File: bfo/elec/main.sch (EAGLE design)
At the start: 10 parts, among them Q1 BC108B

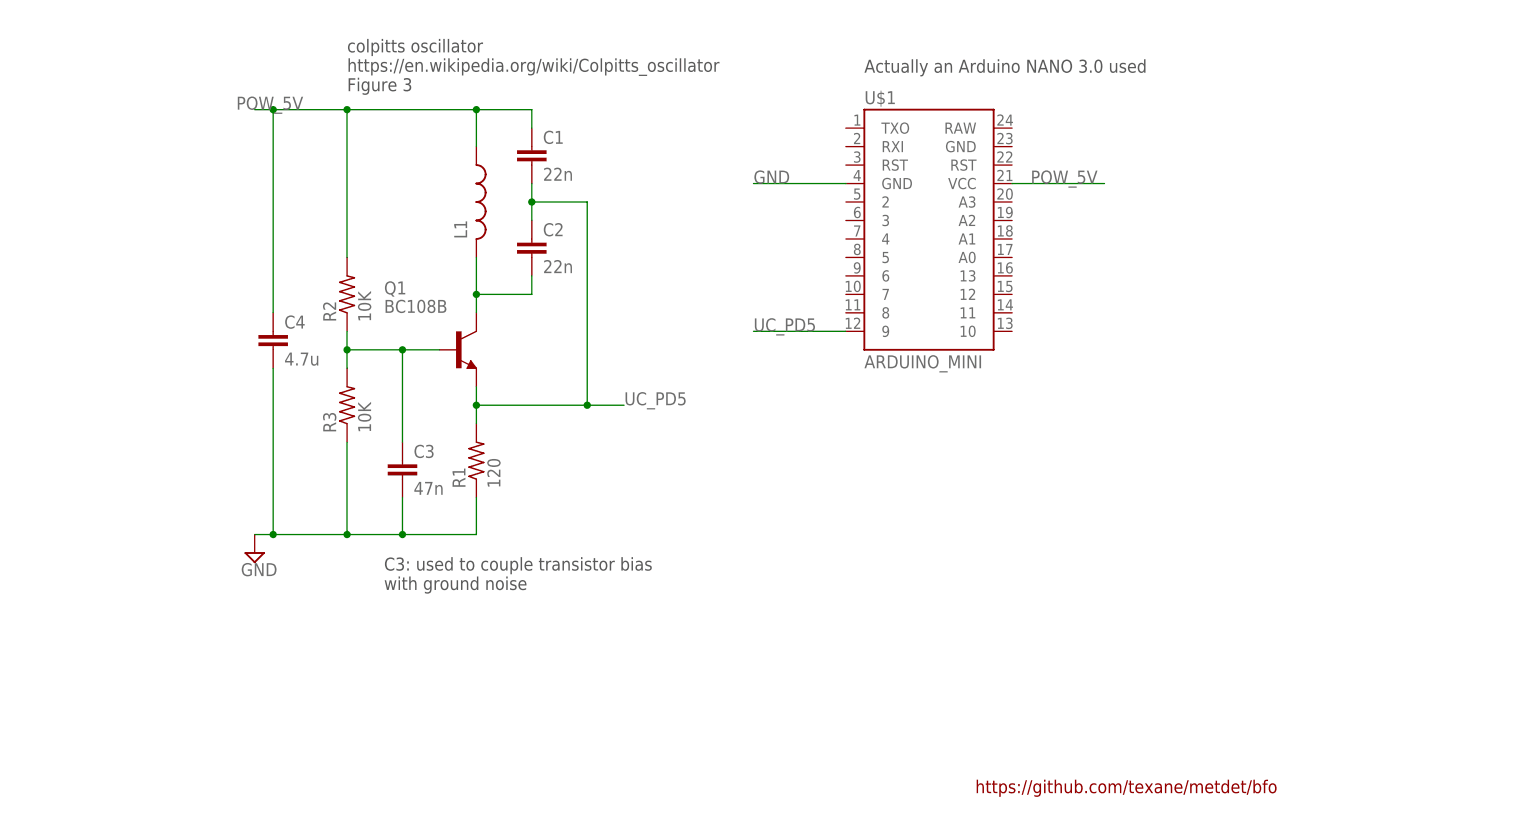
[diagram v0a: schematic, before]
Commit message: bfo/elec: add inverter stage
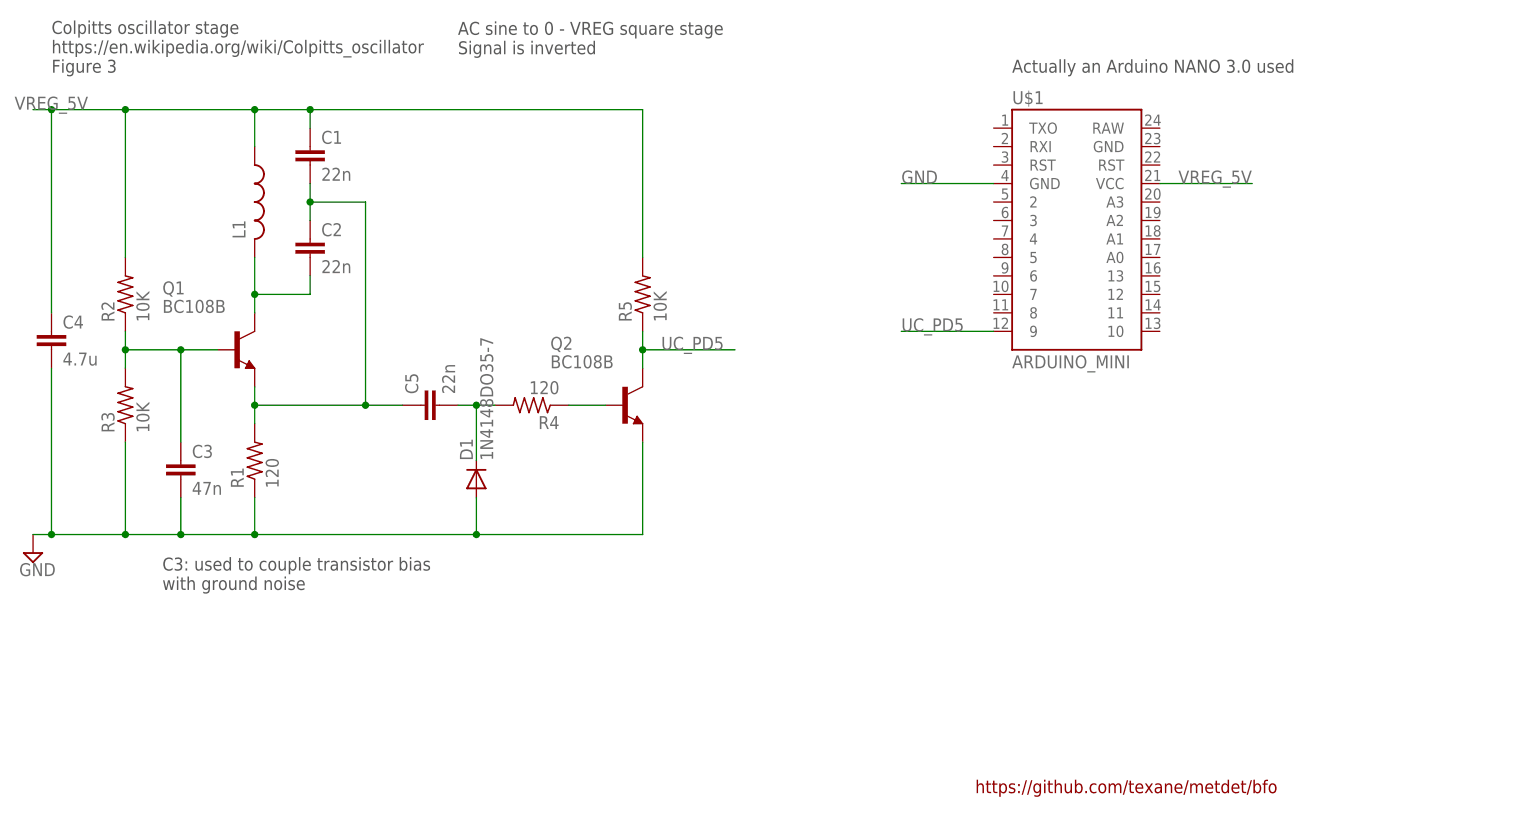
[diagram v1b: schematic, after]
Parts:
- added C5: 22n, rcl:C-EU025-024X044
- added D1: 1N4148DO35-7, diode:1N4148DO35-7
- added Q2: BC108B, transistor-npn:BC108B
- added R4: 120, rcl:R-US_0204/2V
- added R5: 10K, rcl:R-US_0204/2V
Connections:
- removed net POW_5V: C1.1, C4.1, L1.1, R2.2, U$1.VCC
- new net N$10: C1.2, C2.1, C5.1, Q1.E, R1.2
- new net N$5: Q2.B, R4.1
- new net N$6: C5.2, D1.C, R4.2
- new net VREG_5V: C1.1, C4.1, L1.1, R2.2, R5.2, U$1.VCC
- net GND: now also D1.A, Q2.E
- net UC_PD5: now also Q2.C, R5.1; no longer C1.2, C2.1, Q1.E, R1.2
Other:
- note added: "AC sine to 0 - VREG square stage Signal is inverted"
- note added: "Colpitts oscillator stage https://en.wikipedia.org/wiki/Colpitts_oscillator Figure 3"
- note removed: "colpitts oscillator https://en.wikipedia.org/wiki/Colpitts_oscillator Figure 3"
- moved on the sheet: C1, C2, C3, C4, L1, Q1, R1, R2, R3, U$1

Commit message: bfo/elec: comments
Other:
- note added: "AC sine to logic (0 - VREG, inverted)"
- note removed: "AC sine to 0 - VREG square stage Signal is inverted"
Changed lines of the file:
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@@
 <text x="114.3" y="58.42" size="1.778" layer="97">Actually an Arduino NANO 3.0 used</text>
 <text x="109.22" y="-40.64" size="1.778" layer="94">https://github.com/texane/metdet/bfo</text>
-<text x="38.1" y="60.96" size="1.778" layer="97">AC sine to 0 - VREG square stage
-Signal is inverted</text>
+<text x="38.1" y="58.42" size="1.778" layer="97">AC sine to logic (0 - VREG, inverted)</text>
 </plain>
 <instances>

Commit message: bfo/elec: add piezo buzzer
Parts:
- added SG1: EFBAA40D101, buzzer:EFBAA40D101
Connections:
- new net N$2: SG1.1, U$1.10
- net GND: now also SG1.2
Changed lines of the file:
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@@
 <part name="Q2" library="transistor-npn" deviceset="BC108B" device=""/>
 <part name="D1" library="diode" deviceset="1N4148" device="DO35-7"/>
+<part name="SG1" library="buzzer" deviceset="EFB?" device="AA40D101"/>
+<part name="SUPPLY2" library="supply2" deviceset="GND" device=""/>
 </parts>
 <sheets>
@@
 <instance part="Q2" gate="G$1" x="60.96" y="12.7"/>
 <instance part="D1" gate="G$1" x="40.64" y="2.54" rot="R90"/>
+<instance part="SG1" gate="G$1" x="144.78" y="25.4"/>
+<instance part="SUPPLY2" gate="GND" x="160.02" y="20.32"/>
 </instances>
 <busses>
@@
 <label x="99.06" y="43.18" size="1.778" layer="95"/>
 </segment>
+<segment>
+<pinref part="SG1" gate="G$1" pin="2"/>
+<wire x1="149.86" y1="22.86" x2="160.02" y2="22.86" width="0.1524" layer="91"/>
+<pinref part="SUPPLY2" gate="GND" pin="GND"/>
+</segment>
 </net>
 <net name="VREG_5V" class="0">
@@
 </segment>
 </net>
+<net name="N$2" class="0">
+<segment>
+<pinref part="U$1" gate="G$1" pin="10"/>
+<pinref part="SG1" gate="G$1" pin="1"/>
+<wire x1="134.62" y1="22.86" x2="142.24" y2="22.86" width="0.1524" layer="91"/>
+</segment>
+</net>

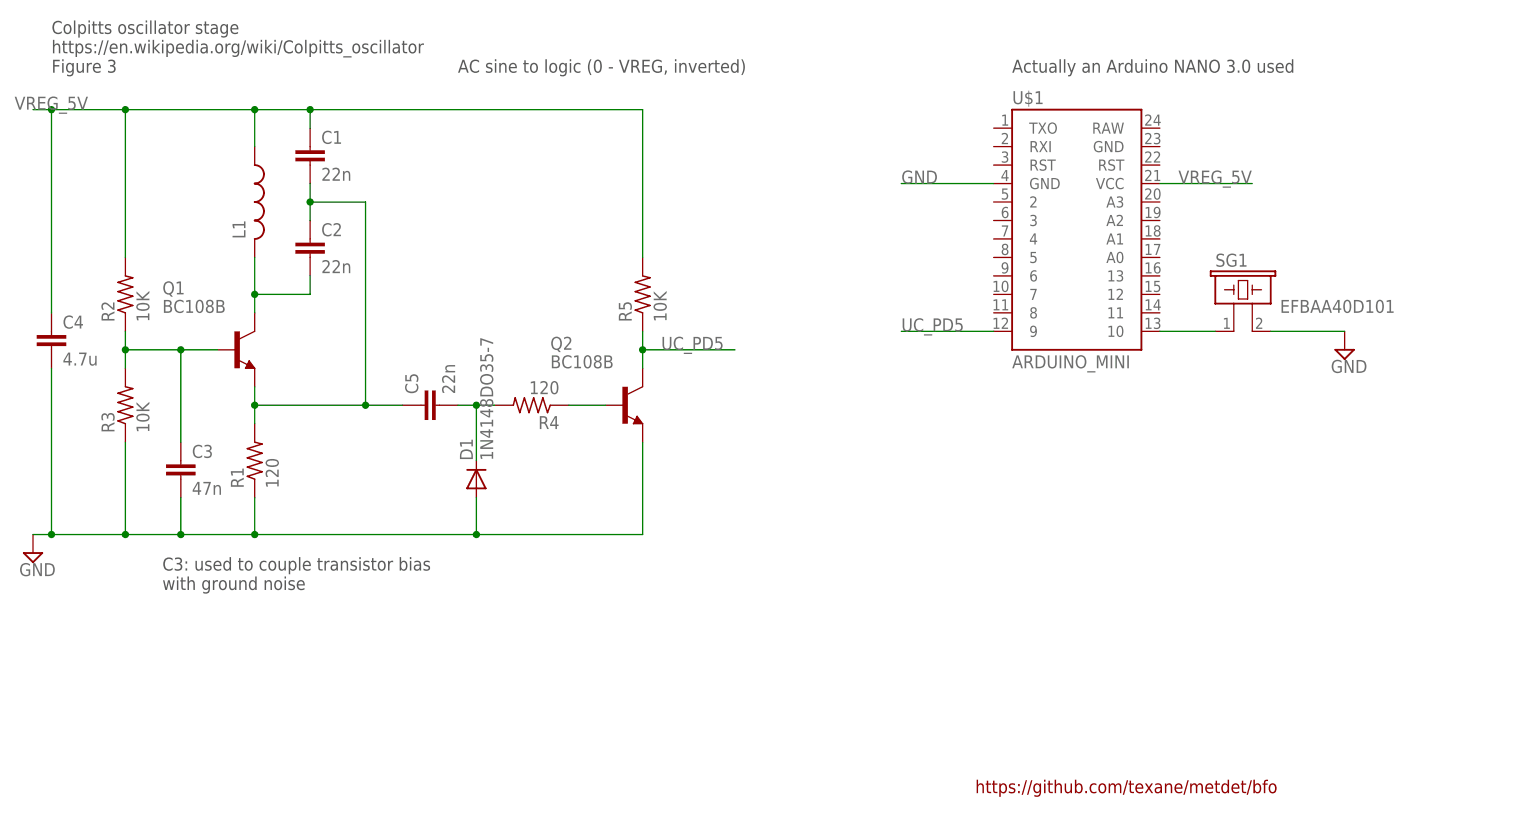
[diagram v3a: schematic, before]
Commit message: bfo/elec: add box connector
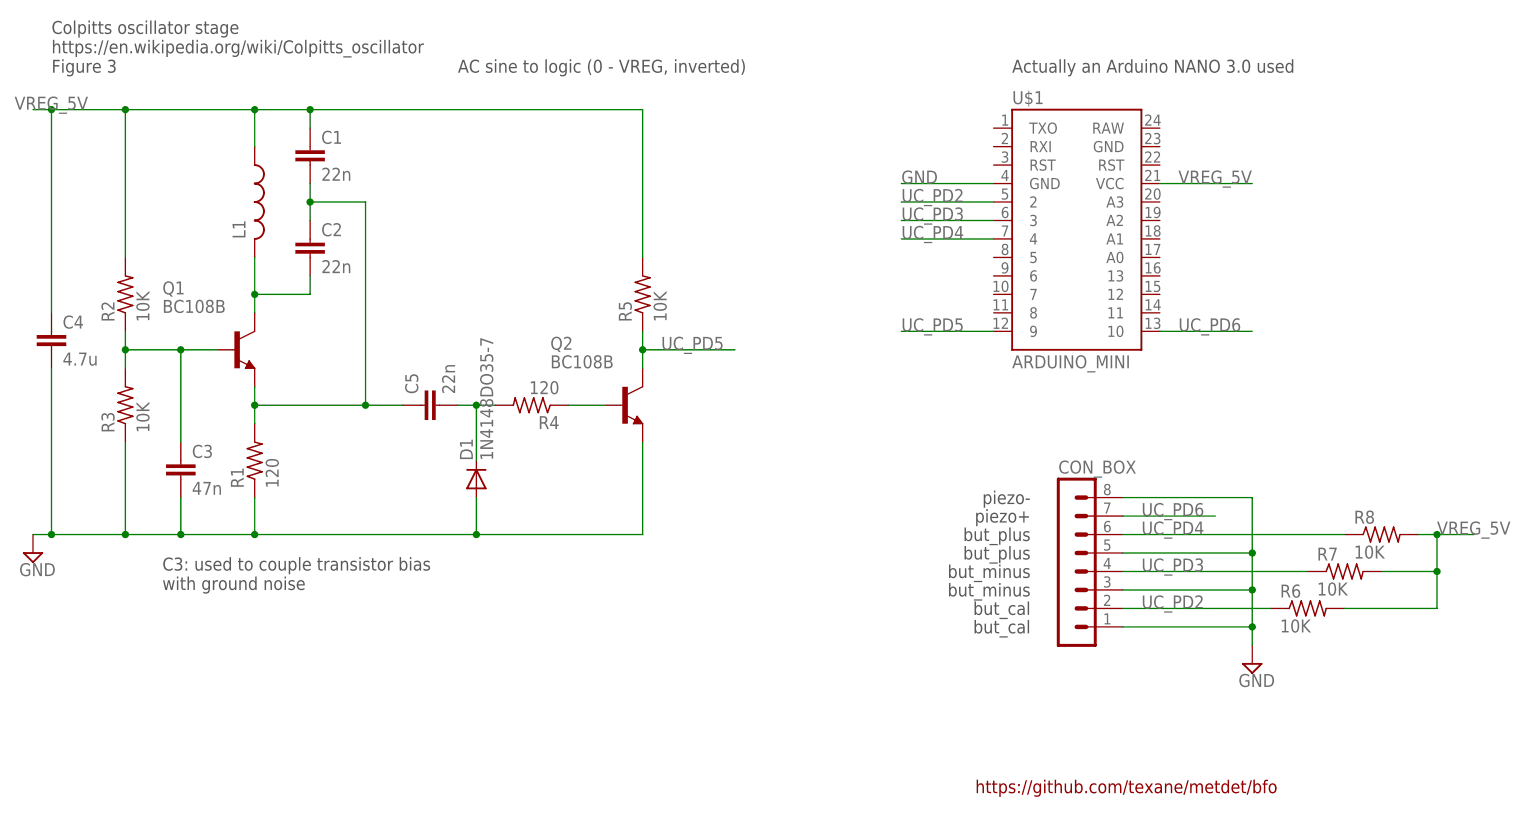
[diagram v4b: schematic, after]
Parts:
- removed SG1: EFBAA40D101, buzzer:EFBAA40D101
- added CON_BOX: (no value), con-lstb:MA08-1
- added R6, R7, R8: 10K, rcl:R-US_0204/2V
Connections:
- removed net N$2: SG1.1, U$1.10
- new net UC_PD2: CON_BOX.2, R6.1, U$1.2
- new net UC_PD3: CON_BOX.4, R7.1, U$1.3
- new net UC_PD4: CON_BOX.6, R8.1, U$1.4
- new net UC_PD6: CON_BOX.7, U$1.10
- net GND: now also CON_BOX.1, CON_BOX.3, CON_BOX.5, CON_BOX.8; no longer SG1.2
- net VREG_5V: now also R6.2, R7.2, R8.2
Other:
- note added: "but_cal"
- note added: "but_minus"
- note added: "but_plus"
- note added: "piezo+"
- note added: "piezo-"
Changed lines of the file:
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@@
 <part name="Q2" library="transistor-npn" deviceset="BC108B" device=""/>
 <part name="D1" library="diode" deviceset="1N4148" device="DO35-7"/>
-<part name="SG1" library="buzzer" deviceset="EFB?" device="AA40D101"/>
-<part name="SUPPLY2" library="supply2" deviceset="GND" device=""/>
+<part name="CON_BOX" library="con-lstb" deviceset="MA08-1" device=""/>
+<part name="R6" library="rcl" deviceset="R-US_" device="0204/2V" value="10K"/>
+<part name="R7" library="rcl" deviceset="R-US_" device="0204/2V" value="10K"/>
+<part name="R8" library="rcl" deviceset="R-US_" device="0204/2V" value="10K"/>
+<part name="SUPPLY4" library="supply2" deviceset="GND" device=""/>
 </parts>
 <sheets>
@@
 <text x="109.22" y="-40.64" size="1.778" layer="94">https://github.com/texane/metdet/bfo</text>
 <text x="38.1" y="58.42" size="1.778" layer="97">AC sine to logic (0 - VREG, inverted)</text>
+<text x="116.84" y="0" size="1.778" layer="97" align="center-right">piezo-</text>
+<text x="116.84" y="-2.54" size="1.778" layer="97" align="center-right">piezo+</text>
+<text x="116.84" y="-5.08" size="1.778" layer="97" align="center-right">but_plus</text>
+<text x="116.84" y="-7.62" size="1.778" layer="97" align="center-right">but_plus</text>
+<text x="116.84" y="-10.16" size="1.778" layer="97" align="center-right">but_minus</text>
+<text x="116.84" y="-12.7" size="1.778" layer="97" align="center-right">but_minus</text>
+<text x="116.84" y="-15.24" size="1.778" layer="97" align="center-right">but_cal</text>
+<text x="116.84" y="-17.78" size="1.778" layer="97" align="center-right">but_cal</text>
 </plain>
 <instances>
@@
 <instance part="Q2" gate="G$1" x="60.96" y="12.7"/>
 <instance part="D1" gate="G$1" x="40.64" y="2.54" rot="R90"/>
-<instance part="SG1" gate="G$1" x="144.78" y="25.4"/>
-<instance part="SUPPLY2" gate="GND" x="160.02" y="20.32"/>
+<instance part="CON_BOX" gate="1" x="121.92" y="-10.16"/>
+<instance part="R6" gate="G$1" x="154.94" y="-15.24"/>
+<instance part="R7" gate="G$1" x="160.02" y="-10.16"/>
+<instance part="R8" gate="G$1" x="165.1" y="-5.08"/>
+<instance part="SUPPLY4" gate="GND" x="147.32" y="-22.86"/>
 </instances>
 <busses>
@@
 </segment>
 <segment>
-<pinref part="SG1" gate="G$1" pin="2"/>
-<wire x1="149.86" y1="22.86" x2="160.02" y2="22.86" width="0.1524" layer="91"/>
-<pinref part="SUPPLY2" gate="GND" pin="GND"/>
+<pinref part="CON_BOX" gate="1" pin="5"/>
+<wire x1="129.54" y1="-7.62" x2="147.32" y2="-7.62" width="0.1524" layer="91"/>
+<pinref part="SUPPLY4" gate="GND" pin="GND"/>
+<wire x1="147.32" y1="-7.62" x2="147.32" y2="-12.7" width="0.1524" layer="91"/>
+<pinref part="CON_BOX" gate="1" pin="3"/>
+<wire x1="147.32" y1="-12.7" x2="147.32" y2="-17.78" width="0.1524" layer="91"/>
+<wire x1="147.32" y1="-17.78" x2="147.32" y2="-20.32" width="0.1524" layer="91"/>
+<wire x1="129.54" y1="-12.7" x2="147.32" y2="-12.7" width="0.1524" layer="91"/>
+<junction x="147.32" y="-12.7"/>
+<pinref part="CON_BOX" gate="1" pin="1"/>
+<wire x1="129.54" y1="-17.78" x2="147.32" y2="-17.78" width="0.1524" layer="91"/>
+<junction x="147.32" y="-17.78"/>
+<pinref part="CON_BOX" gate="1" pin="8"/>
+<wire x1="129.54" y1="0" x2="147.32" y2="0" width="0.1524" layer="91"/>
+<wire x1="147.32" y1="0" x2="147.32" y2="-7.62" width="0.1524" layer="91"/>
+<junction x="147.32" y="-7.62"/>
 </segment>
 </net>
@@
 <label x="137.16" y="43.18" size="1.778" layer="95"/>
 </segment>
+<segment>
+<pinref part="R8" gate="G$1" pin="2"/>
+<wire x1="170.18" y1="-5.08" x2="172.72" y2="-5.08" width="0.1524" layer="91"/>
+<wire x1="172.72" y1="-5.08" x2="172.72" y2="-10.16" width="0.1524" layer="91"/>
+<pinref part="R6" gate="G$1" pin="2"/>
+<wire x1="172.72" y1="-10.16" x2="172.72" y2="-15.24" width="0.1524" layer="91"/>
+<wire x1="172.72" y1="-15.24" x2="160.02" y2="-15.24" width="0.1524" layer="91"/>
+<pinref part="R7" gate="G$1" pin="2"/>
+<wire x1="165.1" y1="-10.16" x2="172.72" y2="-10.16" width="0.1524" layer="91"/>
+<junction x="172.72" y="-10.16"/>
+<wire x1="172.72" y1="-5.08" x2="177.8" y2="-5.08" width="0.1524" layer="91"/>
+<junction x="172.72" y="-5.08"/>
+<label x="172.72" y="-5.08" size="1.778" layer="95"/>
+</segment>
 </net>
 <net name="N$10" class="0">
@@
 </segment>
 </net>
-<net name="N$2" class="0">
+<net name="UC_PD6" class="0">
+<segment>
+<pinref part="CON_BOX" gate="1" pin="7"/>
+<wire x1="129.54" y1="-2.54" x2="142.24" y2="-2.54" width="0.1524" layer="91"/>
+<label x="132.08" y="-2.54" size="1.778" layer="95"/>
+</segment>
 <segment>
 <pinref part="U$1" gate="G$1" pin="10"/>
-<pinref part="SG1" gate="G$1" pin="1"/>
-<wire x1="134.62" y1="22.86" x2="142.24" y2="22.86" width="0.1524" layer="91"/>
-</segment>
-</net>
+<wire x1="134.62" y1="22.86" x2="147.32" y2="22.86" width="0.1524" layer="91"/>
+<label x="137.16" y="22.86" size="1.778" layer="95"/>
+</segment>
+</net>
+<net name="UC_PD2" class="0">
+<segment>
+<pinref part="U$1" gate="G$1" pin="2"/>
+<wire x1="111.76" y1="40.64" x2="99.06" y2="40.64" width="0.1524" layer="91"/>
+<label x="99.06" y="40.64" size="1.778" layer="95"/>
+</segment>
+<segment>
+<pinref part="R6" gate="G$1" pin="1"/>
+<pinref part="CON_BOX" gate="1" pin="2"/>
+<wire x1="149.86" y1="-15.24" x2="129.54" y2="-15.24" width="0.1524" layer="91"/>
+<label x="132.08" y="-15.24" size="1.778" layer="95"/>
+</segment>
+</net>
+<net name="UC_PD3" class="0">
+<segment>
+<pinref part="U$1" gate="G$1" pin="3"/>
+<wire x1="111.76" y1="38.1" x2="99.06" y2="38.1" width="0.1524" layer="91"/>
+<label x="99.06" y="38.1" size="1.778" layer="95"/>
+</segment>
+<segment>
+<pinref part="R7" gate="G$1" pin="1"/>
+<pinref part="CON_BOX" gate="1" pin="4"/>
+<wire x1="154.94" y1="-10.16" x2="129.54" y2="-10.16" width="0.1524" layer="91"/>
+<label x="132.08" y="-10.16" size="1.778" layer="95"/>
+</segment>
+</net>
+<net name="UC_PD4" class="0">
+<segment>
+<pinref part="U$1" gate="G$1" pin="4"/>
+<wire x1="111.76" y1="35.56" x2="99.06" y2="35.56" width="0.1524" layer="91"/>
+<label x="99.06" y="35.56" size="1.778" layer="95"/>
+</segment>
+<segment>
+<pinref part="CON_BOX" gate="1" pin="6"/>
+<wire x1="160.02" y1="-5.08" x2="129.54" y2="-5.08" width="0.1524" layer="91"/>
+<pinref part="R8" gate="G$1" pin="1"/>
+<label x="132.08" y="-5.08" size="1.778" layer="95"/>
+</segment>
+</net>
